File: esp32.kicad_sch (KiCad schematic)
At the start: 21 parts, among them J2 TC2030-IDC, J3 Conn_01x04, J4 Conn_01x06, J5 USB_C_Receptacle_USB2.0, SW1 GT-TC029B-H025-L1N, SW2 GT-TC029B-H025-L1N, U3 RT9080-33GJ5, U4 ESP32-S3-WROOM-1

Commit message: lots of misc
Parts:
- removed C25: 0.1uF, Capacitor_SMD:C_0402_1005Metric, symbol Device:C
- TP10, TP11, TP5, TP6, TP7, TP9: footprint TestPoint:TestPoint_Pad_D1.5mm -> TestPoint:TestPoint_Pad_D2.5mm
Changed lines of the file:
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@@
-	(wire
-		(pts
-			(xy 132.715 66.04) (xy 132.715 68.58)
-		)
-		(stroke
-			(width 0)
-			(type default)
-		)
-	)
 	(wire
 		(pts
@@
 		(pts
 			(xy 184.912 37.465) (xy 191.77 37.465)
-		)
-		(stroke
-			(width 0)
-			(type default)
-		)
-	)
-	(wire
-		(pts
-			(xy 132.715 58.42) (xy 132.715 55.88)
 		)
 		(stroke
@@
 				(path "/e63e39d7-6ac0-4ffd-8aa3-1841a4541b55/ca857324-2ec8-447e-bd58-90d0c2e6b6d7"
 					(reference "J4")
-					(unit 1)
-				)
-			)
-		)
-	)
-	(symbol
-		(lib_id "Device:C")
-		(at 132.715 62.23 0)
-		(unit 1)
-		(exclude_from_sim no)
-		(in_bom yes)
-		(on_board yes)
-		(dnp no)
-		(fields_autoplaced yes)
-		(property "Reference" "C25"
-			(at 136.525 60.9599 0)
-			(effects
-				(font
-					(size 1.27 1.27)
-				)
-				(justify left)
-			)
-		)
-		(property "Value" "0.1uF"
-			(at 136.525 63.4999 0)
-			(effects
-				(font
-					(size 1.27 1.27)
-				)
-				(justify left)
-			)
-		)
-		(property "Footprint" "Capacitor_SMD:C_0402_1005Metric"
-			(at 133.6802 66.04 0)
-			(effects
-				(font
-					(size 1.27 1.27)
-				)
-				(hide yes)
-			)
-		)
-		(property "Datasheet" ""
-			(at 132.715 62.23 0)
-			(effects
-				(font
-					(size 1.27 1.27)
-				)
-				(hide yes)
-			)
-		)
-		(property "Description" ""
-			(at 132.715 62.23 0)
-			(effects
-				(font
-					(size 1.27 1.27)
-				)
-				(hide yes)
-			)
-		)
-		(property "DK" "1276-1234-1-ND"
-			(at 132.715 62.23 0)
-			(effects
-				(font
-					(size 1.27 1.27)
-				)
-				(hide yes)
-			)
-		)
-		(property "PARTNO" "CL05A104KO5NNNC"
-			(at 132.715 62.23 0)
-			(effects
-				(font
-					(size 1.27 1.27)
-				)
-				(hide yes)
-			)
-		)
-		(pin "1"
-		)
-		(pin "2"
-		)
-		(instances
-			(project "bitaxeGamma"
-				(path "/e63e39d7-6ac0-4ffd-8aa3-1841a4541b55/ca857324-2ec8-447e-bd58-90d0c2e6b6d7"
-					(reference "C25")
 					(unit 1)
 				)
@@
 			)
 		)
-		(property "Footprint" "TestPoint:TestPoint_Pad_D1.5mm"
+		(property "Footprint" "TestPoint:TestPoint_Pad_D2.5mm"
 			(at 52.07 173.99 0)
 			(effects
@@
 			)
 		)
-		(property "Footprint" "TestPoint:TestPoint_Pad_D1.5mm"
+		(property "Footprint" "TestPoint:TestPoint_Pad_D2.5mm"
 			(at 80.01 166.37 0)
 			(effects
@@
 			)
 		)
-		(property "Footprint" "TestPoint:TestPoint_Pad_D1.5mm"
+		(property "Footprint" "TestPoint:TestPoint_Pad_D2.5mm"
 			(at 80.01 161.29 0)
 			(effects
@@
 			)
 		)
-		(property "Footprint" "TestPoint:TestPoint_Pad_D1.5mm"
+		(property "Footprint" "TestPoint:TestPoint_Pad_D2.5mm"
 			(at 80.01 163.83 0)
 			(effects
@@
 			)
 		)
-		(property "Footprint" "TestPoint:TestPoint_Pad_D1.5mm"
+		(property "Footprint" "TestPoint:TestPoint_Pad_D2.5mm"
 			(at 52.07 171.45 0)
 			(effects
@@
 			)
 		)
-		(property "Footprint" "TestPoint:TestPoint_Pad_D1.5mm"
+		(property "Footprint" "TestPoint:TestPoint_Pad_D2.5mm"
 			(at 52.07 176.53 0)
 			(effects

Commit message: inductor change
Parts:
- removed C24: 10uF, Capacitor_SMD:C_0805_2012Metric, symbol Device:C
- added C6: 10uF, Capacitor_SMD:C_0603_1608Metric, symbol Device:C_Small
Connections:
- net 3V3: now also C6.1
- net GND: now also C6.2
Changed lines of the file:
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@@
+	(wire
+		(pts
+			(xy 121.92 63.5) (xy 121.92 68.58)
+		)
+		(stroke
+			(width 0)
+			(type default)
+		)
+	)
 	(wire
 		(pts
@@
 		(pts
 			(xy 35.56 90.805) (xy 35.56 92.075)
-		)
-		(stroke
-			(width 0)
-			(type default)
-		)
-	)
-	(wire
-		(pts
-			(xy 121.92 68.58) (xy 121.92 66.04)
 		)
 		(stroke
@@
 	)
 	(symbol
+		(lib_id "Device:C_Small")
+		(at 121.92 60.96 0)
+		(unit 1)
+		(exclude_from_sim no)
+		(in_bom yes)
+		(on_board yes)
+		(dnp no)
+		(property "Reference" "C6"
+			(at 128.016 60.198 0)
+			(effects
+				(font
+					(size 1.27 1.27)
+				)
+				(justify right)
+			)
+		)
+		(property "Value" "10uF"
+			(at 128.016 62.484 0)
+			(effects
+				(font
+					(size 1.27 1.27)
+				)
+				(justify right)
+			)
+		)
+		(property "Footprint" "Capacitor_SMD:C_0603_1608Metric"
+			(at 121.92 60.96 0)
+			(effects
+				(font
+					(size 1.27 1.27)
+				)
+				(hide yes)
+			)
+		)
+		(property "Datasheet" "~"
+			(at 121.92 60.96 0)
+			(effects
+				(font
+					(size 1.27 1.27)
+				)
+				(hide yes)
+			)
+		)
+		(property "Description" "Unpolarized capacitor, small symbol"
+			(at 121.92 60.96 0)
+			(effects
+				(font
+					(size 1.27 1.27)
+				)
+				(hide yes)
+			)
+		)
+		(property "PARTNO" "GRM188R61E106KA73D"
+			(at 121.92 60.96 0)
+			(effects
+				(font
+					(size 1.27 1.27)
+				)
+				(hide yes)
+			)
+		)
+		(property "DK" "490-18214-1-ND"
+			(at 121.92 60.96 0)
+			(effects
+				(font
+					(size 1.27 1.27)
+				)
+				(hide yes)
+			)
+		)
+		(property "partnum" ""
+			(at 121.92 60.96 0)
+			(effects
+				(font
+					(size 1.27 1.27)
+				)
+				(hide yes)
+			)
+		)
+		(pin "1"
+		)
+		(pin "2"
+		)
+		(instances
+			(project "bitaxeGamma"
+				(path "/e63e39d7-6ac0-4ffd-8aa3-1841a4541b55/ca857324-2ec8-447e-bd58-90d0c2e6b6d7"
+					(reference "C6")
+					(unit 1)
+				)
+			)
+		)
+	)
+	(symbol
 		(lib_id "bitaxe:TC2030-IDC-NL")
 		(at 66.04 168.91 0)
@@
 					(unit 1)
 				)
-			)
-		)
-	)
-	(symbol
-		(lib_id "Device:C")
-		(at 121.92 62.23 0)
-		(unit 1)
-		(exclude_from_sim no)
-		(in_bom yes)
-		(on_board yes)
-		(dnp no)
-		(fields_autoplaced yes)
-		(property "Reference" "C24"
-			(at 125.095 60.9599 0)
-			(effects
-				(font
-					(size 1.27 1.27)
-				)
-				(justify left)
-			)
-		)
-		(property "Value" "10uF"
-			(at 125.095 63.4999 0)
-			(effects
-				(font
-					(size 1.27 1.27)
-				)
-				(justify left)
-			)
-		)
-		(property "Footprint" "Capacitor_SMD:C_0805_2012Metric"
-			(at 122.8852 66.04 0)
-			(effects
-				(font
-					(size 1.27 1.27)
-				)
-				(hide yes)
-			)
-		)
-		(property "Datasheet" ""
-			(at 121.92 62.23 0)
-			(effects
-				(font
-					(size 1.27 1.27)
-				)
-				(hide yes)
-			)
-		)
-		(property "Description" ""
-			(at 121.92 62.23 0)
-			(effects
-				(font
-					(size 1.27 1.27)
-				)
-				(hide yes)
-			)
-		)
-		(property "DK" "1276-1096-1-ND"
-			(at 121.92 62.23 0)
-			(effects
-				(font
-					(size 1.27 1.27)
-				)
-				(hide yes)
-			)
-		)
-		(property "PARTNO" "CL21A106KOQNNNE"
-			(at 121.92 62.23 0)
-			(effects
-				(font
-					(size 1.27 1.27)
-				)
-				(hide yes)
-			)
-		)
-		(pin "1"
-		)
-		(pin "2"
-		)
-		(instances
-			(project "bitaxeGamma"
-				(path "/e63e39d7-6ac0-4ffd-8aa3-1841a4541b55/ca857324-2ec8-447e-bd58-90d0c2e6b6d7"
-					(reference "C24")
-					(unit 1)
-				)

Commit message: remove incorrect J3 partno for #28. removed random dust from mounting hole positions for #32. bumped version to 603. added NRSTO pulldown. added NRSTI pulldown for #36. removed old manufacturing files.
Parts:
- J3: DK S5596-ND -> (none); PARTNO NPTC041KFXC-RC -> (none)
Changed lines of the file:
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@@
 	(title_block
 		(title "bitaxeGamma")
-		(date "2024-09-26")
-		(rev "602")
+		(date "2025-04-29")
+		(rev "603")
 	)
 	(text "Accessory Port"
@@
 			)
 		)
-		(property "DK" "S5596-ND"
-			(at 0 64.77 0)
-			(effects
-				(font
-					(size 1.27 1.27)
-				)
-				(hide yes)
-			)
-		)
-		(property "PARTNO" "NPTC041KFXC-RC"
-			(at 0 64.77 0)
-			(effects
-				(font
-					(size 1.27 1.27)
-				)
-				(hide yes)
-			)
-		)
 		(property "HEIGHT" ""
 			(at 196.85 32.385 0)
 			(effects
-				(font
-					(size 1.27 1.27)
-				)
-			)
-		)
-		(property "Mouser" ""
-			(at 196.85 32.385 0)
-			(effects

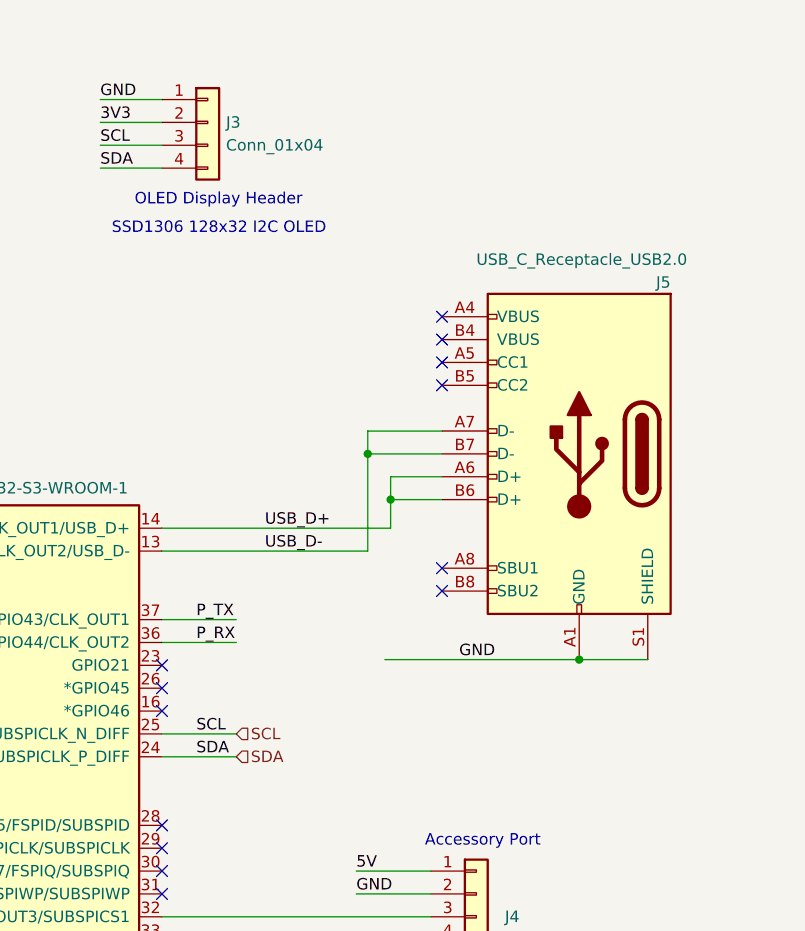
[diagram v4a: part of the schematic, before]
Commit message: added pullup resistors for #25
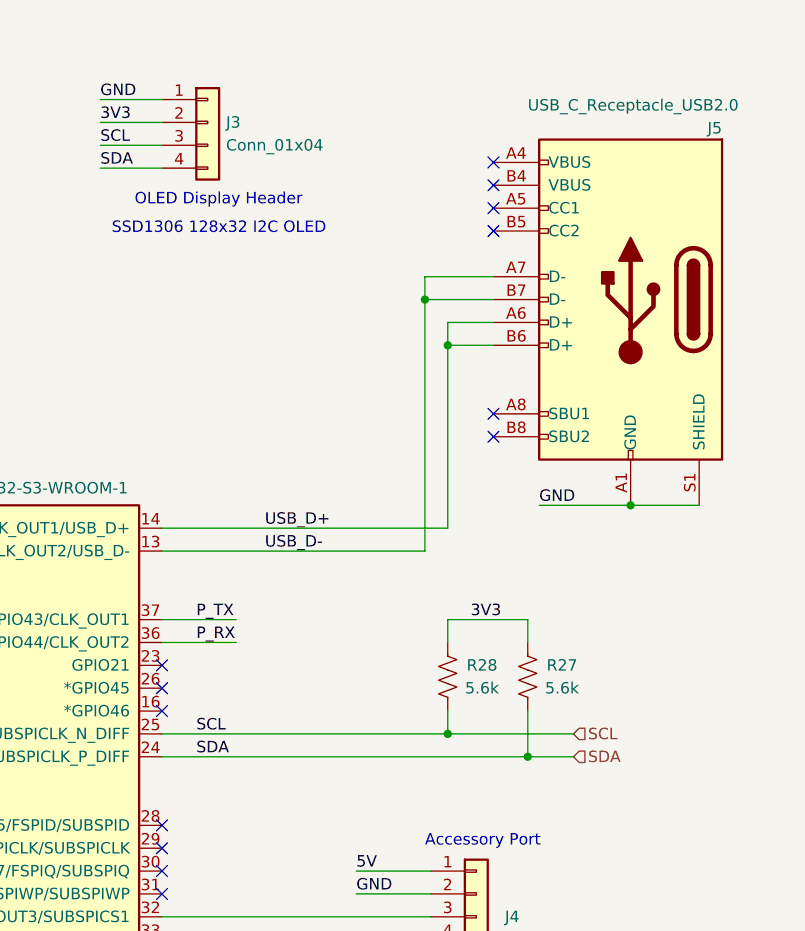
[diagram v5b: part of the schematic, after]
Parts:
- added R27, R28: 5.6k, Resistor_SMD:R_0402_1005Metric, symbol Device:R_US
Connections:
- net 3V3: now also R27.2, R28.2
- net SCL: now also R28.1
- net SDA: now also R27.1
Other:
- moved on the sheet: J5

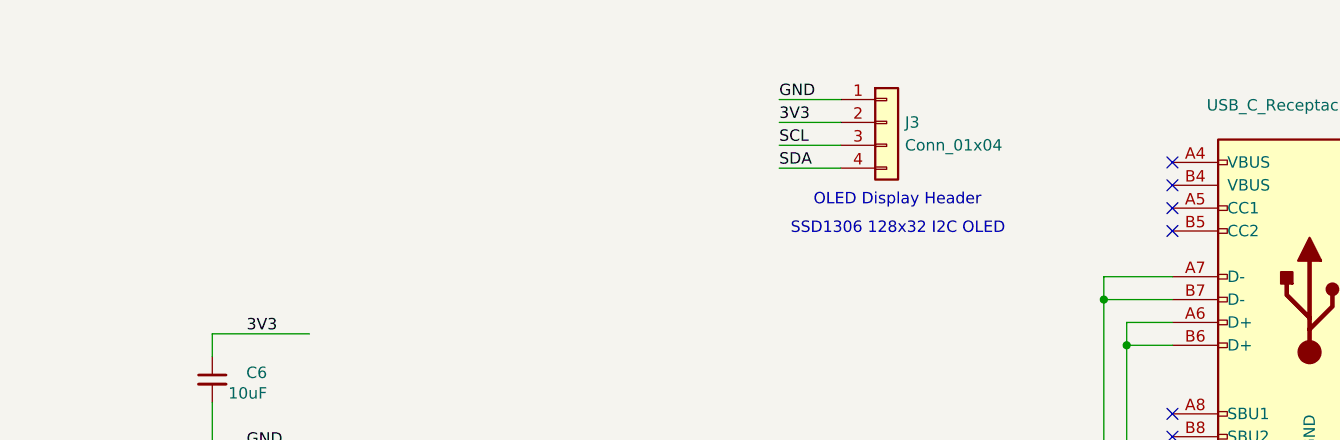
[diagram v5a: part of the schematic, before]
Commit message: added USB ID pulldown resistors for #37
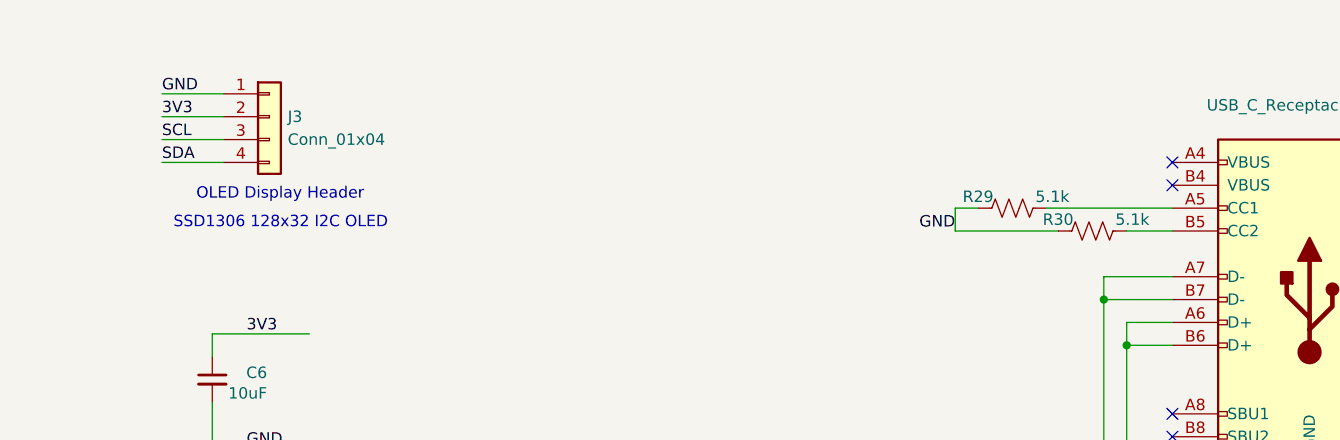
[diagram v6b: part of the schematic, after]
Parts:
- added R29, R30: 5.1k, Resistor_SMD:R_0402_1005Metric, symbol Device:R_US
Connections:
- net GND: now also R29.1, R30.1
- net at J5.A5 (CC1): now also R29.2
- net at J5.B5 (CC2): now also R30.2
- no-connect marks 24 -> 22
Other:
- moved on the sheet: J3

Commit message: init
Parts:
- removed TP8: TestPoint, TestPoint:TestPoint_Pad_D1.5mm, symbol Connector:TestPoint
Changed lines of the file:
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@@
-	(symbol
-		(lib_id "Connector:TestPoint")
-		(at 66.04 135.89 90)
-		(mirror x)
-		(unit 1)
-		(exclude_from_sim no)
-		(in_bom no)
-		(on_board yes)
-		(dnp no)
-		(property "Reference" "TP8"
-			(at 59.69 135.89 90)
-			(effects
-				(font
-					(size 1.27 1.27)
-				)
-			)
-		)
-		(property "Value" "TestPoint"
-			(at 60.325 137.1599 90)
-			(effects
-				(font
-					(size 1.27 1.27)
-				)
-				(justify left)
-				(hide yes)
-			)
-		)
-		(property "Footprint" "TestPoint:TestPoint_Pad_D1.5mm"
-			(at 66.04 140.97 0)
-			(effects
-				(font
-					(size 1.27 1.27)
-				)
-				(hide yes)
-			)
-		)
-		(property "Datasheet" "~"
-			(at 66.04 140.97 0)
-			(effects
-				(font
-					(size 1.27 1.27)
-				)
-				(hide yes)
-			)
-		)
-		(property "Description" ""
-			(at 66.04 135.89 0)
-			(effects
-				(font
-					(size 1.27 1.27)
-				)
-				(hide yes)
-			)
-		)
-		(property "HEIGHT" ""
-			(at 66.04 135.89 0)
-			(effects
-				(font
-					(size 1.27 1.27)
-				)
-			)
-		)
-		(property "Mouser" ""
-			(at 66.04 135.89 0)
-			(effects
-				(font
-					(size 1.27 1.27)
-				)
-			)
-		)
-		(pin "1"
-		)
-		(instances
-			(project "bitaxeGamma"
-				(path "/e63e39d7-6ac0-4ffd-8aa3-1841a4541b55/ca857324-2ec8-447e-bd58-90d0c2e6b6d7"
-					(reference "TP8")
-					(unit 1)
-				)
-			)
-		)
-	)
 	(symbol
 		(lib_id "Connector:TestPoint")
